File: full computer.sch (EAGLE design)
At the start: 66 parts, among them IC2 74HC541N, IC3 74HC573N, IC4 74HC04N

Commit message: moved PS2 to rear side and BREAK button to front side, the board is now a bit smaller
Signed-off-by: Panagiotis Varelas <varelaspanos@gmail.com>
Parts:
- JP1: value (none) -> AUDIO
- U$39: value MINI-DIN6 -> KEYBOARD
- U$40: value DSUB15 -> MONITOR
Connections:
- net GND: now also JP2.GND, JP2.GNDBREAK; no longer JP2.PWR
- net VCC: now also JP2.PWR; no longer JP2.GND
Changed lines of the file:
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@@
 <part name="SUPPLY22" library="supply2" deviceset="GND" device=""/>
 <part name="SUPPLY23" library="supply2" deviceset="GND" device=""/>
-<part name="U$39" library="SparkFun-Connectors" deviceset="MINI-DIN6" device="PTH" value="MINI-DIN6"/>
-<part name="U$40" library="SparkFun-Connectors" deviceset="DB15" device="" value="DSUB15"/>
-<part name="JP1" library="SparkFun-Connectors" deviceset="AUDIO-JACK" device="2.5MM"/>
+<part name="U$39" library="SparkFun-Connectors" deviceset="MINI-DIN6" device="PTH" value="KEYBOARD"/>
+<part name="U$40" library="SparkFun-Connectors" deviceset="DB15" device="" value="MONITOR"/>
+<part name="JP1" library="SparkFun-Connectors" deviceset="AUDIO-JACK" device="2.5MM" value="AUDIO"/>
 <part name="JP2" library="SparkFun-Connectors" deviceset="POWER_JACK" device="PTH" value="POWER 5V"/>
 <part name="SUPPLY8" library="supply2" deviceset="GND" device=""/>
@@
 </segment>
 <segment>
+<pinref part="C9" gate="G$1" pin="+"/>
+<pinref part="C8" gate="G$1" pin="+"/>
+<wire x1="132.08" y1="256.54" x2="142.24" y2="256.54" width="0.1524" layer="91"/>
+<junction x="132.08" y="256.54"/>
+<pinref part="C6" gate="G$1" pin="1"/>
 <pinref part="SUPPLY17" gate="G$1" pin="VCC"/>
-<pinref part="C6" gate="G$1" pin="1"/>
 <wire x1="119.38" y1="259.08" x2="119.38" y2="256.54" width="0.1524" layer="91"/>
 <junction x="119.38" y="256.54"/>
-<pinref part="C8" gate="G$1" pin="+"/>
 <wire x1="119.38" y1="256.54" x2="132.08" y2="256.54" width="0.1524" layer="91"/>
-<pinref part="C9" gate="G$1" pin="+"/>
-<wire x1="132.08" y1="256.54" x2="142.24" y2="256.54" width="0.1524" layer="91"/>
-<junction x="132.08" y="256.54"/>
-<pinref part="JP2" gate="G$1" pin="GND"/>
-<wire x1="68.58" y1="248.92" x2="109.22" y2="248.92" width="0.1524" layer="91"/>
-<wire x1="109.22" y1="248.92" x2="109.22" y2="256.54" width="0.1524" layer="91"/>
-<wire x1="109.22" y1="256.54" x2="119.38" y2="256.54" width="0.1524" layer="91"/>
+<wire x1="119.38" y1="256.54" x2="76.2" y2="256.54" width="0.1524" layer="91"/>
+<wire x1="76.2" y1="256.54" x2="76.2" y2="254" width="0.1524" layer="91"/>
+<pinref part="JP2" gate="G$1" pin="PWR"/>
+<wire x1="76.2" y1="254" x2="68.58" y2="254" width="0.1524" layer="91"/>
 </segment>
 <segment>
@@
 <wire x1="119.38" y1="248.92" x2="119.38" y2="246.38" width="0.1524" layer="91"/>
 <junction x="119.38" y="248.92"/>
-<wire x1="119.38" y1="248.92" x2="111.76" y2="248.92" width="0.1524" layer="91"/>
-<wire x1="111.76" y1="248.92" x2="111.76" y2="254" width="0.1524" layer="91"/>
-<pinref part="JP2" gate="G$1" pin="PWR"/>
-<wire x1="111.76" y1="254" x2="68.58" y2="254" width="0.1524" layer="91"/>
-</segment>
-<segment>
+<pinref part="JP2" gate="G$1" pin="GND"/>
+<wire x1="68.58" y1="248.92" x2="114.3" y2="248.92" width="0.1524" layer="91"/>
+<pinref part="JP2" gate="G$1" pin="GNDBREAK"/>
+<wire x1="114.3" y1="248.92" x2="119.38" y2="248.92" width="0.1524" layer="91"/>
+<wire x1="68.58" y1="251.46" x2="114.3" y2="251.46" width="0.1524" layer="91"/>
+<wire x1="114.3" y1="251.46" x2="114.3" y2="248.92" width="0.1524" layer="91"/>
+<junction x="114.3" y="248.92"/>
+</segment>
+<segment>

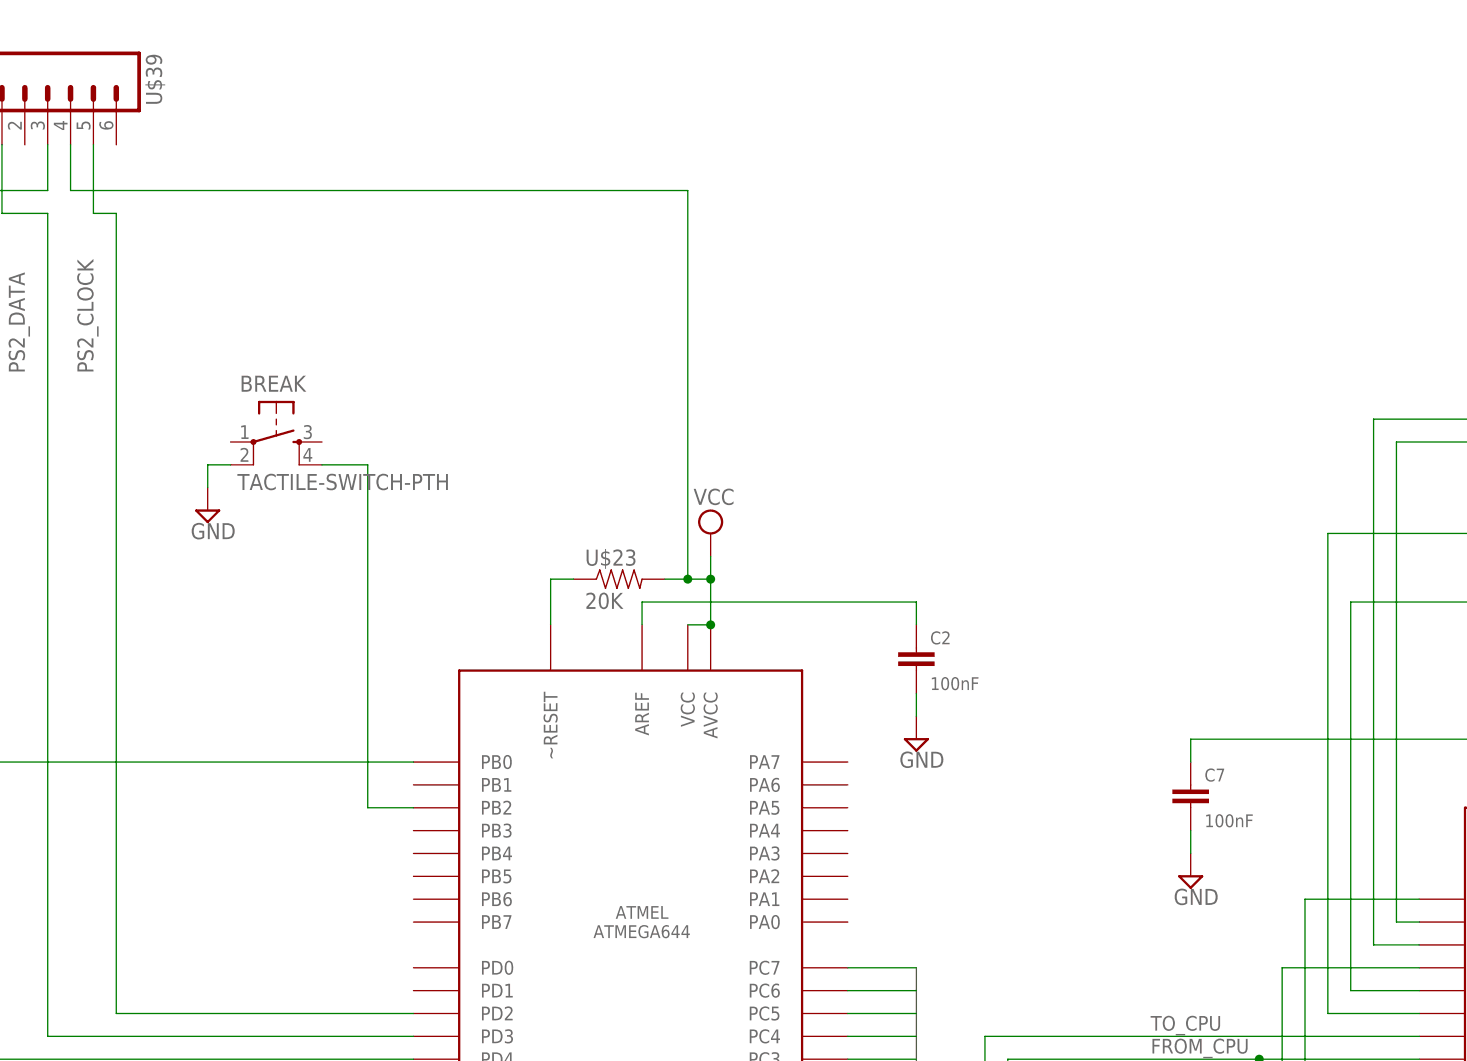
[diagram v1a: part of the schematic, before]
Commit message: added SD card holder & rounded corners
Signed-off-by: Panagiotis Varelas <varelaspanos@gmail.com>
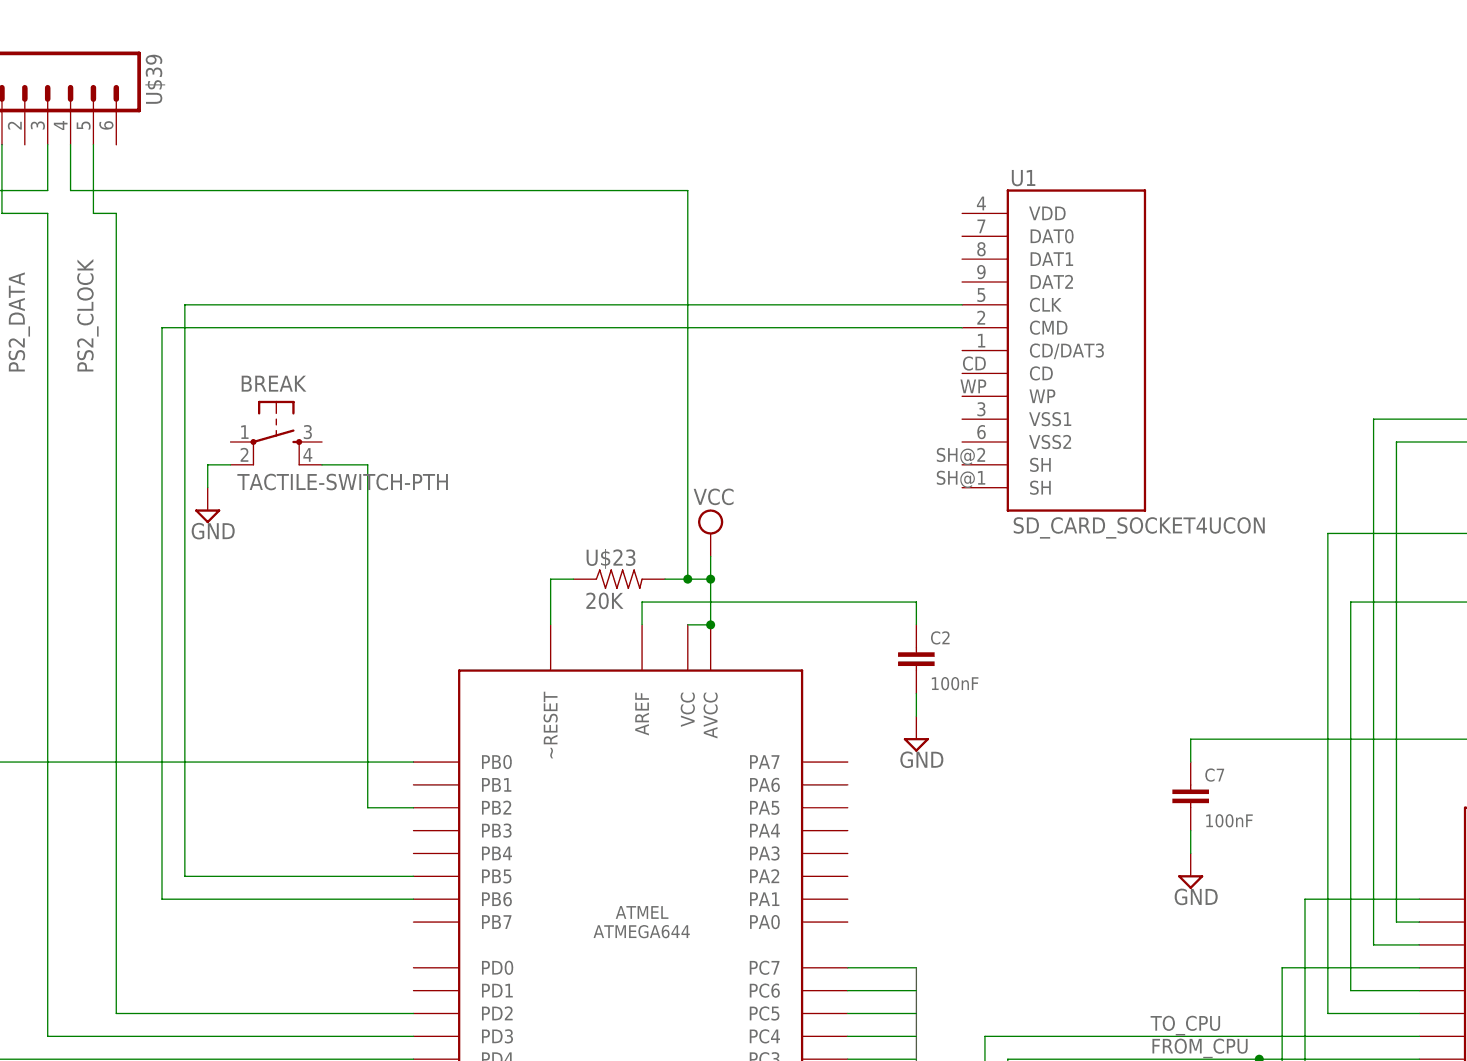
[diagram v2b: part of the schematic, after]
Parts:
- added U1: SD_CARD_SOCKET4UCON, SparkFun-Connectors:SD_CARD_SOCKET4UCON
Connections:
- new net N$47: U$1.PB5, U1.CLK
- new net N$48: U$1.PB6, U1.CMD
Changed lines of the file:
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@@
 <part name="SUPPLY24" library="supply2" deviceset="GND" device=""/>
 <part name="SUPPLY25" library="supply2" deviceset="GND" device=""/>
+<part name="U1" library="SparkFun-Connectors" deviceset="SD_CARD_SOCKET" device="4UCON"/>
 </parts>
 <sheets>
@@
 <instance part="SUPPLY24" gate="GND" x="238.76" y="322.58"/>
 <instance part="SUPPLY25" gate="GND" x="269.24" y="307.34"/>
+<instance part="U1" gate="G$1" x="256.54" y="365.76"/>
 </instances>
 <busses>
@@
 </segment>
 </net>
+<net name="N$47" class="0">
+<segment>
+<pinref part="U1" gate="G$1" pin="CLK"/>
+<wire x1="243.84" y1="370.84" x2="157.48" y2="370.84" width="0.1524" layer="91"/>
+<wire x1="157.48" y1="370.84" x2="157.48" y2="307.34" width="0.1524" layer="91"/>
+<pinref part="U$1" gate="G$1" pin="PB5"/>
+<wire x1="157.48" y1="307.34" x2="182.88" y2="307.34" width="0.1524" layer="91"/>
+</segment>
+</net>
+<net name="N$48" class="0">
+<segment>
+<pinref part="U1" gate="G$1" pin="CMD"/>
+<wire x1="243.84" y1="368.3" x2="154.94" y2="368.3" width="0.1524" layer="91"/>
+<wire x1="154.94" y1="368.3" x2="154.94" y2="304.8" width="0.1524" layer="91"/>
+<pinref part="U$1" gate="G$1" pin="PB6"/>
+<wire x1="154.94" y1="304.8" x2="182.88" y2="304.8" width="0.1524" layer="91"/>
+</segment>
+</net>

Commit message: removed SD card holder & added external SRAM & reverse voltage protection
Signed-off-by: Panagiotis Varelas <varelaspanos@gmail.com>
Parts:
- removed C6: 100nF, capacitor-wima:C5/2.5
- removed U1: SD_CARD_SOCKET4UCON, SparkFun-Connectors:SD_CARD_SOCKET4UCON
- added JMP1: UART, con-lstb:MA03-1
- added Q1: IRF9530, transistor-power:IRF9530
- U$10: value 20K -> 23LC1024; device SparkFun-Resistors:RESISTORPTH-1/4W -> pvar_parts:23LC1024
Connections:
- new net N$22: JMP1.2, U$1.PD0
- new net N$50: U$1.PB6, U$10.SERIALOUT
- new net N$51: U$1.PB5, U$10.SERIALIN
- new net N$52: U$1.PB4, U$10.~CS
- new net N$53: U$1.PB3, U$10.~HOLD
- net GND: now also JMP1.1, Q1.G, U$10.VSS; no longer C6.2
- net N$17: now also JP2.PWR, Q1.D; no longer U$1.~RESET, U$23.1
- net N$4: now also U$1.~RESET, U$23.1; no longer U$10.1
- net N$47: now also JMP1.3, U$1.PD1; no longer U$1.PB5, U1.CLK
- net N$48: now also U$1.PB7, U$10.SCK; no longer U$1.PB6, U1.CMD
- net VCC: now also Q1.S, U$10.VCC; no longer C6.1, JP2.PWR, U$10.2
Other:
- moved on the sheet: BREAK, C8, C9, JP2

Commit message: board completely redesigned!
Signed-off-by: Panagiotis Varelas <varelaspanos@gmail.com>
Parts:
- removed BREAK: TACTILE-SWITCH-PTH, GeekAmmo:TACTILE-SWITCH-PTH
- removed BUZZER: BUZZERNS, SparkFun-Electromechanical:BUZZERNS
- removed C4: 6.8uF, rcl:CPOL-EUE5-5
- removed C7: 100nF, capacitor-wima:C5/2.5
- removed JMP: (no value), con-lstb:MA03-1
- removed JP1: AUDIO, SparkFun-Connectors:AUDIO-JACK2.5MM
- added C6: 100nF, SparkFun-Capacitors:CAPEZ
- added D1: (no value), SparkFun-LED:LED5MM
- added GPIO: 22-23-2081, con-molex:22-23-2081
- added ISP: (no value), con-ml:ML6
- added S1, S3: 9450-2, switch-misc:9450-2
- added S2: (no value), switch-omron:31-XX
- added SG1: F/TMB, buzzer:F/TMB
- added X1: 1503_08, con-lumberg:1503_08
- C14, C15: device capacitor-wima:C5/2.5 -> SparkFun-Passives:CAPEZ
- C2, C5: device capacitor-wima:C5/2.5 -> SparkFun-Capacitors:CAPEZ
- JP2: value POWER 5V -> 5V
- LED1: device led:LED5MM -> SparkFun-LED:LED5MM
- U$11, U$12, U$13, U$14, U$15, U$16, U$26, U$27, U$28, U$29, U$30, U$31, U$32, U$33, U$34, U$35, U$36, U$37, U$38, U$4, U$5, U$6, U$7, U$8, U$9: device SparkFun-Resistors:RESISTORPTH-1/4W -> SparkFun-Resistors:RESISTOREZ
- U$23: value 20K -> 220R; device SparkFun-Resistors:RESISTORPTH-1/4W -> SparkFun-Resistors:RESISTOREZ
- U$24: value 1K -> 180R; device SparkFun-Resistors:RESISTORPTH-1/4W -> SparkFun-Resistors:RESISTOREZ
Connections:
- removed net N$46: C7.1, U$2.AREF
- new net N$54: GPIO-2.S, U$1.PA6
- new net N$55: GPIO-3.S, U$1.PA5
- new net N$56: GPIO-4.S, U$1.PA4
- new net N$57: GPIO-5.S, U$1.PA3
- new net N$58: GPIO-6.S, U$1.PA2
- new net N$59: GPIO-7.S, U$1.PA1
- new net N$60: GPIO-8.S, U$1.PA0
- new net N$61: ISP.5, U$1.~RESET
- new net N$64: Q1.D, S31.S, S32.S, U$23.2
- new net N$69: D1.A, U$23.1
- net AUDIO-OUT: now also X1.1, X1.3; no longer JP1.LEFT, JP1.RIGHT
- net DATA0: now also U$3.I/O00; no longer U$3.I/O1
- net DATA1: now also U$3.I/O01; no longer U$3.I/O2
- net DATA2: now also U$3.I/O02; no longer U$3.I/O3
- net DATA3: now also U$3.I/O03; no longer U$3.I/O4
- net DATA4: now also U$3.I/O04; no longer U$3.I/O5
- net DATA5: now also U$3.I/O05; no longer U$3.I/O6
- net DATA6: now also U$3.I/O06; no longer U$3.I/O7
- net DATA7: now also U$3.I/O07; no longer U$3.I/O8
- net GND: now also C6.2, D1.C, ISP.6, S2.P, SG1.-, U$3.CE, X1.2, X1.2@1; no longer BREAK.2, BUZZER.2, C4.-, C7.2, JP1.SLEEVE, U$3.~CE1
- net N$10: now also U$3.WE; no longer U$3.R/W
- net N$17: now also S31.P, S32.P; no longer Q1.D
- net N$18: now also S11.S, SG1.+; no longer BUZZER.1, JMP.3
- net N$19: now also S11.O; no longer JMP.1
- net N$21: now also S11.P; no longer JMP.2
- net N$3: now also U$3.OE; no longer U$3.~OE
- net N$4: now also GPIO-1.S, U$1.PA7; no longer U$1.~RESET, U$2.~RESET, U$23.1
- net N$48: now also ISP.3
- net N$49: now also S2.S; no longer BREAK.4
- net N$50: now also ISP.1
- net N$51: now also ISP.4
- net VCC: now also C6.1, ISP.2, U$3.+3V; no longer C4.+, U$23.2, U$3.VDD
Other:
- moved on the sheet: C13, C2, JMP1, Q1, U$23

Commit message: thiner and shorter traces for clock signals, better position for GPIO and SERIAL, schematic clean up
Signed-off-by: Panagiotis Varelas <varelaspanos@gmail.com>
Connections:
- net GND: now also JMP1.2; no longer JMP1.1
- net N$22: now also JMP1.1; no longer JMP1.2
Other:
- moved on the sheet: C11, C12, C13, C14, C15, C2, C8, C9, D1, IC2, JP2, LED1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
